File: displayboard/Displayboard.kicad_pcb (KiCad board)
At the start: 2 copper layers, 106 x 76 mm, 27 parts, among them IC401 PCAL6416AHF, Q501 NPN, SW401 Button 1, SW402 Button 2, SW403 Button 3, SW404 Button 4, X501 Touch, X502 Display, X503 Mainboard

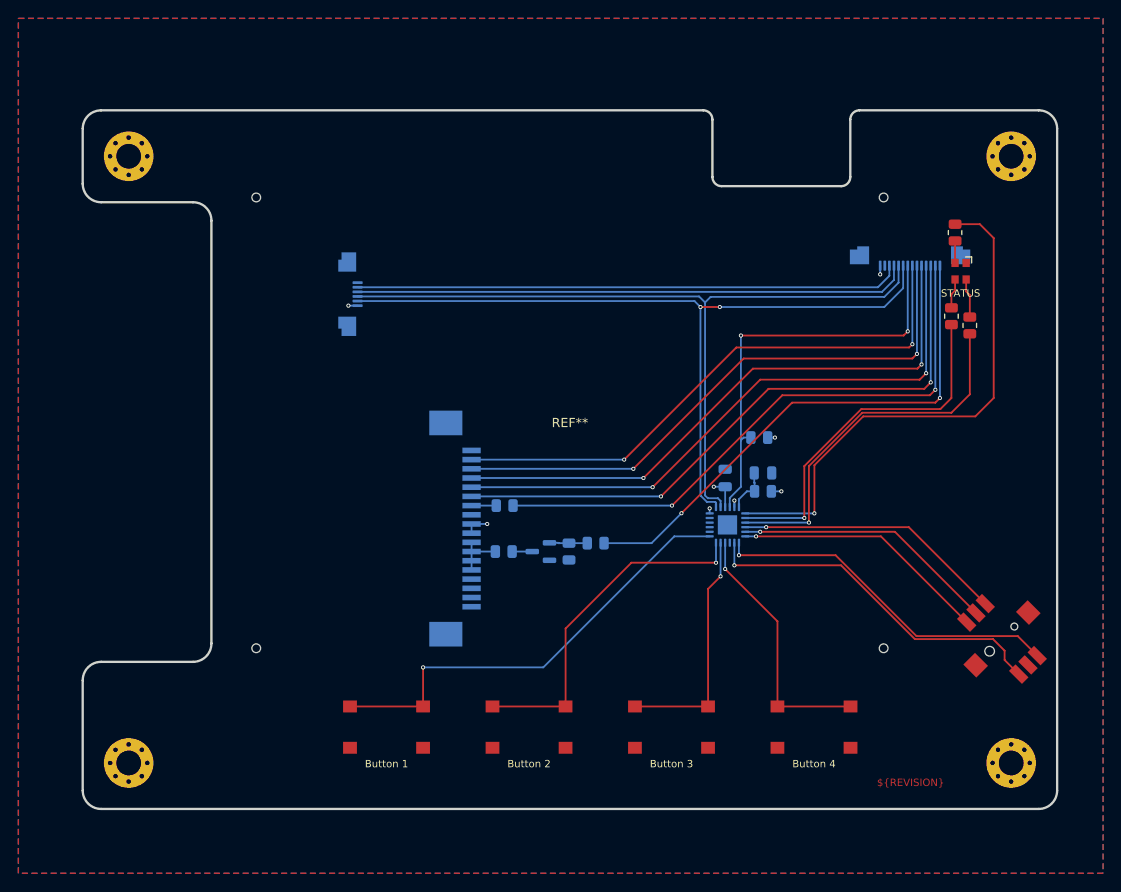
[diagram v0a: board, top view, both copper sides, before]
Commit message: Increase PCB size by 4 mm
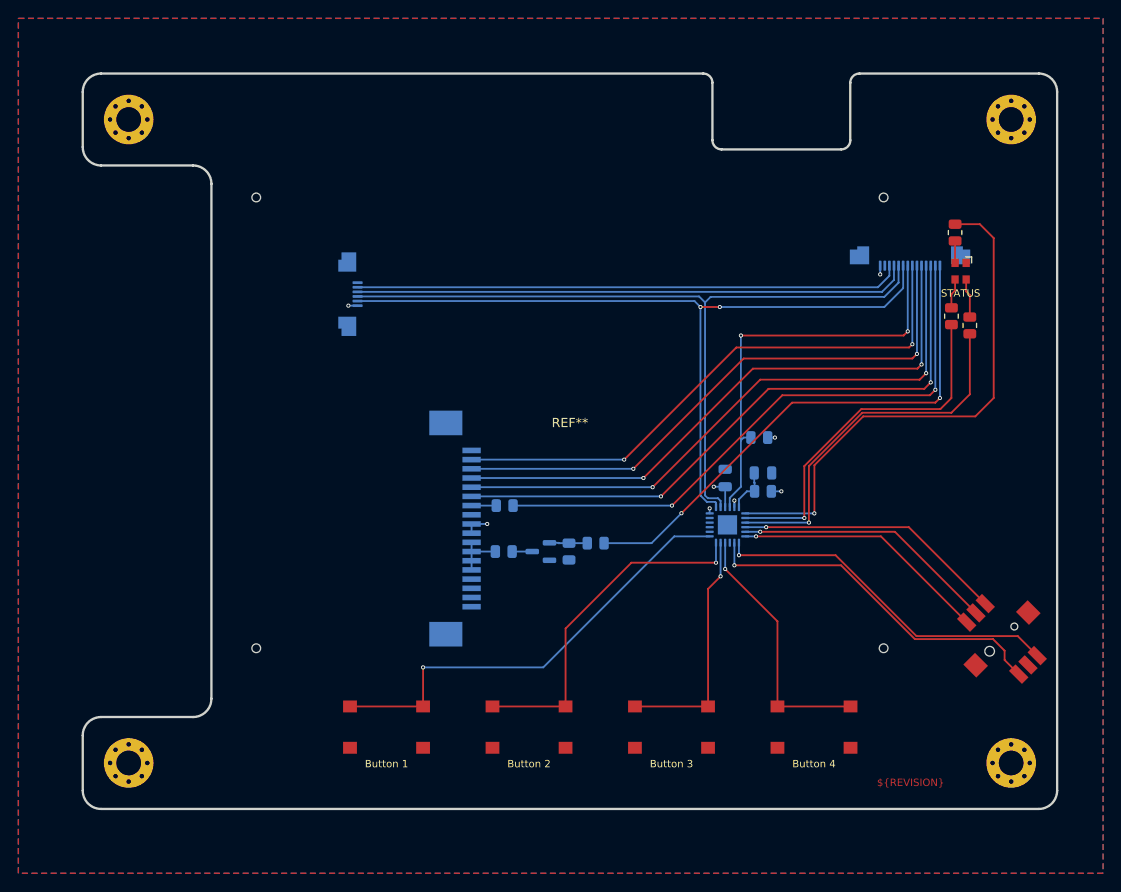
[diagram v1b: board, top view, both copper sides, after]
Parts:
- moved REF** 4.00 mm to (255.5, 79.5)
- moved REF** 4.00 mm to (159.5, 79.5)
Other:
- board size 106 x 76 mm -> 106 x 80 mm
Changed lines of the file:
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@@
 		(locked yes)
 		(layer "F.Cu")
-		(at 255.5 83.5)
+		(at 255.5 79.5)
 		(descr "Mounting Hole 2.7mm")
 		(tags "mounting hole 2.7mm")
@@
 		(locked yes)
 		(layer "F.Cu")
-		(at 159.5 83.5)
+		(at 159.5 79.5)
 		(descr "Mounting Hole 2.7mm")
 		(tags "mounting hole 2.7mm")
@@
 	)
 	(gr_arc
-		(start 222 78.5)
-		(mid 222.707107 78.792893)
-		(end 223 79.5)
+		(start 222 74.5)
+		(mid 222.707107 74.792893)
+		(end 223 75.5)
 		(stroke
 			(width 0.254)
@@
 	)
 	(gr_arc
-		(start 238 79.5)
-		(mid 238.292893 78.792893)
-		(end 239 78.5)
+		(start 238 75.5)
+		(mid 238.292893 74.792893)
+		(end 239 74.5)
 		(stroke
 			(width 0.254)
@@
 	)
 	(gr_line
-		(start 166.5 138.5)
-		(end 156.5 138.5)
+		(start 166.5 144.5)
+		(end 156.5 144.5)
 		(stroke
 			(width 0.254)
@@
 	)
 	(gr_line
-		(start 156.5 88.5)
-		(end 166.5 88.5)
+		(start 156.5 84.5)
+		(end 166.5 84.5)
 		(stroke
 			(width 0.254)
@@
 	)
 	(gr_line
-		(start 154.5 86.5)
-		(end 154.5 80.5)
+		(start 154.5 82.5)
+		(end 154.5 76.5)
 		(stroke
 			(width 0.254)
@@
 	)
 	(gr_arc
-		(start 166.5 88.5)
-		(mid 167.914214 89.085786)
-		(end 168.5 90.5)
+		(start 166.5 84.5)
+		(mid 167.914214 85.085786)
+		(end 168.5 86.5)
 		(stroke
 			(width 0.254)
@@
 	)
 	(gr_arc
-		(start 156.5 88.5)
-		(mid 155.085786 87.914214)
-		(end 154.5 86.5)
+		(start 156.5 84.5)
+		(mid 155.085786 83.914214)
+		(end 154.5 82.5)
 		(stroke
 			(width 0.254)
@@
 	)
 	(gr_arc
-		(start 258.5 78.5)
-		(mid 259.914214 79.085786)
-		(end 260.5 80.5)
+		(start 258.5 74.5)
+		(mid 259.914214 75.085786)
+		(end 260.5 76.5)
 		(stroke
 			(width 0.254)
@@
 	)
 	(gr_arc
-		(start 168.5 136.5)
-		(mid 167.914214 137.914214)
-		(end 166.5 138.5)
+		(start 168.5 142.5)
+		(mid 167.914214 143.914214)
+		(end 166.5 144.5)
 		(stroke
 			(width 0.254)
@@
 	)
 	(gr_arc
-		(start 224 86.75)
-		(mid 223.292893 86.457107)
-		(end 223 85.75)
+		(start 224 82.75)
+		(mid 223.292893 82.457107)
+		(end 223 81.75)
 		(stroke
 			(width 0.254)
@@
 	)
 	(gr_line
-		(start 260.5 80.5)
+		(start 260.5 76.5)
 		(end 260.5 152.5)
 		(stroke
@@
 	)
 	(gr_arc
-		(start 154.5 140.5)
-		(mid 155.085786 139.085786)
-		(end 156.5 138.5)
+		(start 154.5 146.5)
+		(mid 155.085786 145.085786)
+		(end 156.5 144.5)
 		(stroke
 			(width 0.254)
@@
 	)
 	(gr_line
-		(start 222 78.5)
-		(end 156.5 78.5)
+		(start 222 74.5)
+		(end 156.5 74.5)
 		(stroke
 			(width 0.254)
@@
 	)
 	(gr_line
-		(start 168.5 90.5)
-		(end 168.5 136.5)
+		(start 168.5 86.5)
+		(end 168.5 142.5)
 		(stroke
 			(width 0.254)
@@
 	)
 	(gr_line
-		(start 238 85.75)
-		(end 238 79.5)
+		(start 238 81.75)
+		(end 238 75.5)
 		(stroke
 			(width 0.254)
@@
 	)
 	(gr_arc
-		(start 238 85.75)
-		(mid 237.707107 86.457107)
-		(end 237 86.75)
+		(start 238 81.75)
+		(mid 237.707107 82.457107)
+		(end 237 82.75)
 		(stroke
 			(width 0.254)
@@
 	)
 	(gr_line
-		(start 223 85.75)
-		(end 223 79.5)
+		(start 223 81.75)
+		(end 223 75.5)
 		(stroke
 			(width 0.254)
@@
 	)
 	(gr_line
-		(start 224 86.75)
-		(end 237 86.75)
+		(start 224 82.75)
+		(end 237 82.75)
 		(stroke
 			(width 0.254)
@@
 	)
 	(gr_line
-		(start 239 78.5)
-		(end 258.5 78.5)
+		(start 239 74.5)
+		(end 258.5 74.5)
 		(stroke
 			(width 0.254)
@@
 	(gr_line
 		(start 154.5 152.5)
-		(end 154.5 140.5)
+		(end 154.5 146.5)
 		(stroke
 			(width 0.254)
@@
 	)
 	(gr_arc
-		(start 154.5 80.5)
-		(mid 155.085786 79.085786)
-		(end 156.5 78.5)
+		(start 154.5 76.5)
+		(mid 155.085786 75.085786)
+		(end 156.5 74.5)
 		(stroke
 			(width 0.254)
@@
 		(layer "User.6")
 		(pts
-			(xy 222 78.5) (xy 260.5 80.5)
+			(xy 222 74.5) (xy 260.5 76.5)
 		)
 		(height -9.5)
@@
 		)
 		(gr_text "38,5000 mm"
-			(at 241.25 68.08 0)
+			(at 241.25 64.08 0)
 			(layer "User.6")
 			(effects
@@
 		(layer "User.6")
 		(pts
-			(xy 239.8 78.5) (xy 239.8 86.75)
+			(xy 239.8 74.5) (xy 239.8 82.75)
 		)
 		(height 24.2)
@@
 		)
 		(gr_text "8,2500 mm"
-			(at 263.08 82.625 90)
+			(at 263.08 78.625 90)
 			(layer "User.6")
 			(effects
